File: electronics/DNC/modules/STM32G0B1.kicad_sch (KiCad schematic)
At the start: 1 part, among them U4 STM32G0B1RETx

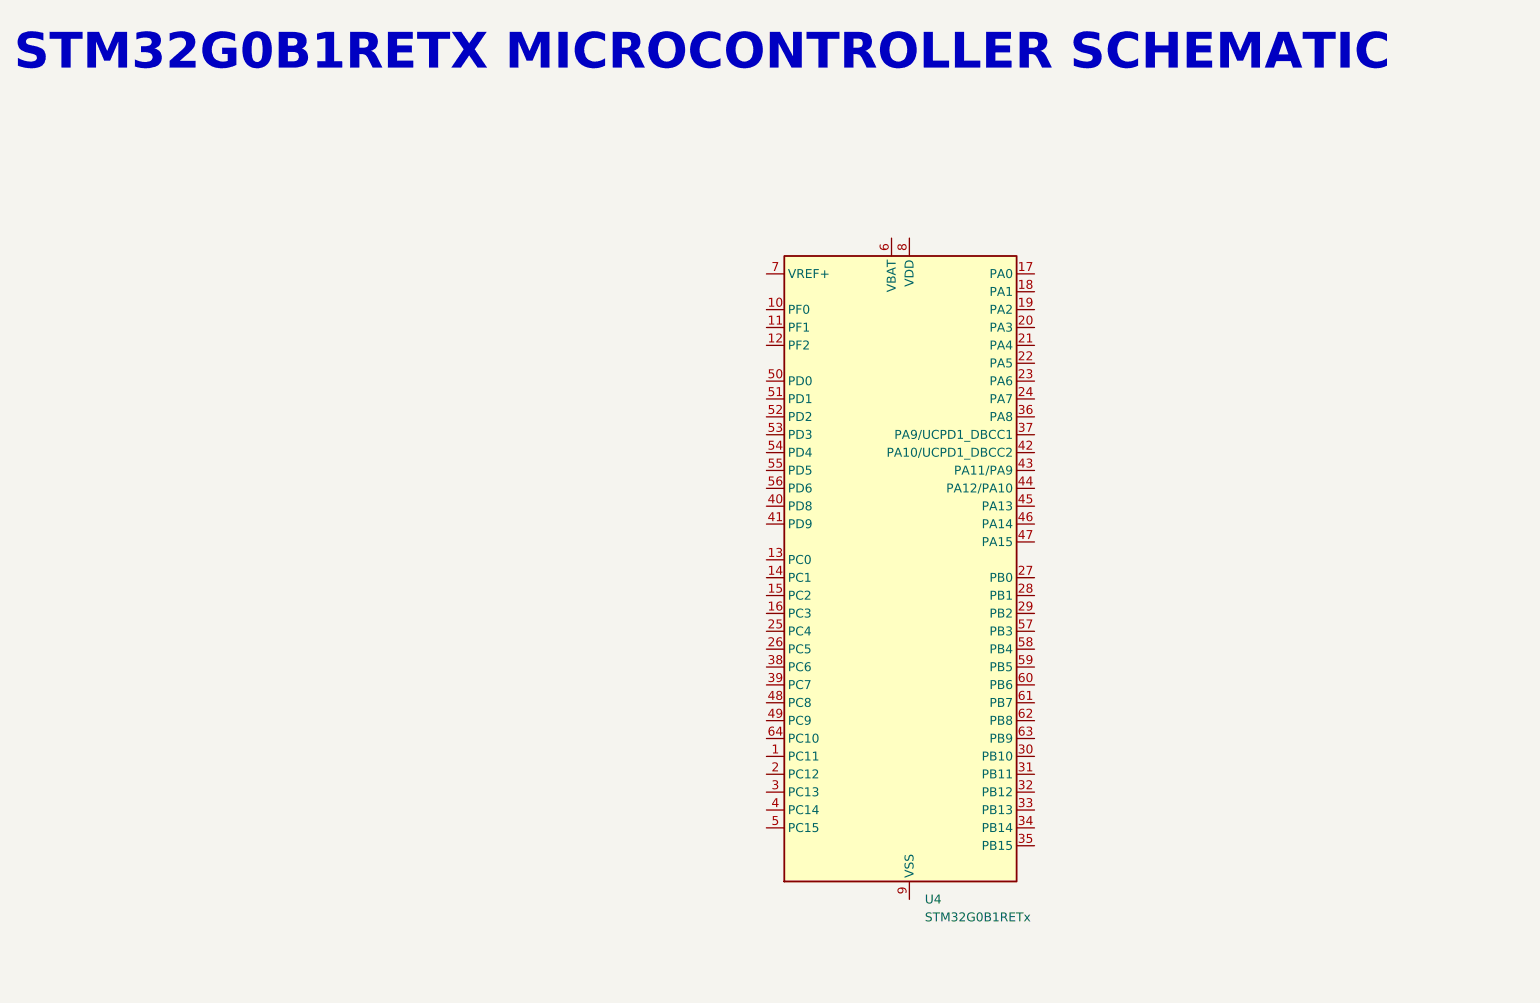
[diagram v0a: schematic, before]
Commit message: Se empezó de nuevo el diseño del DNC con una nueva arquitectura
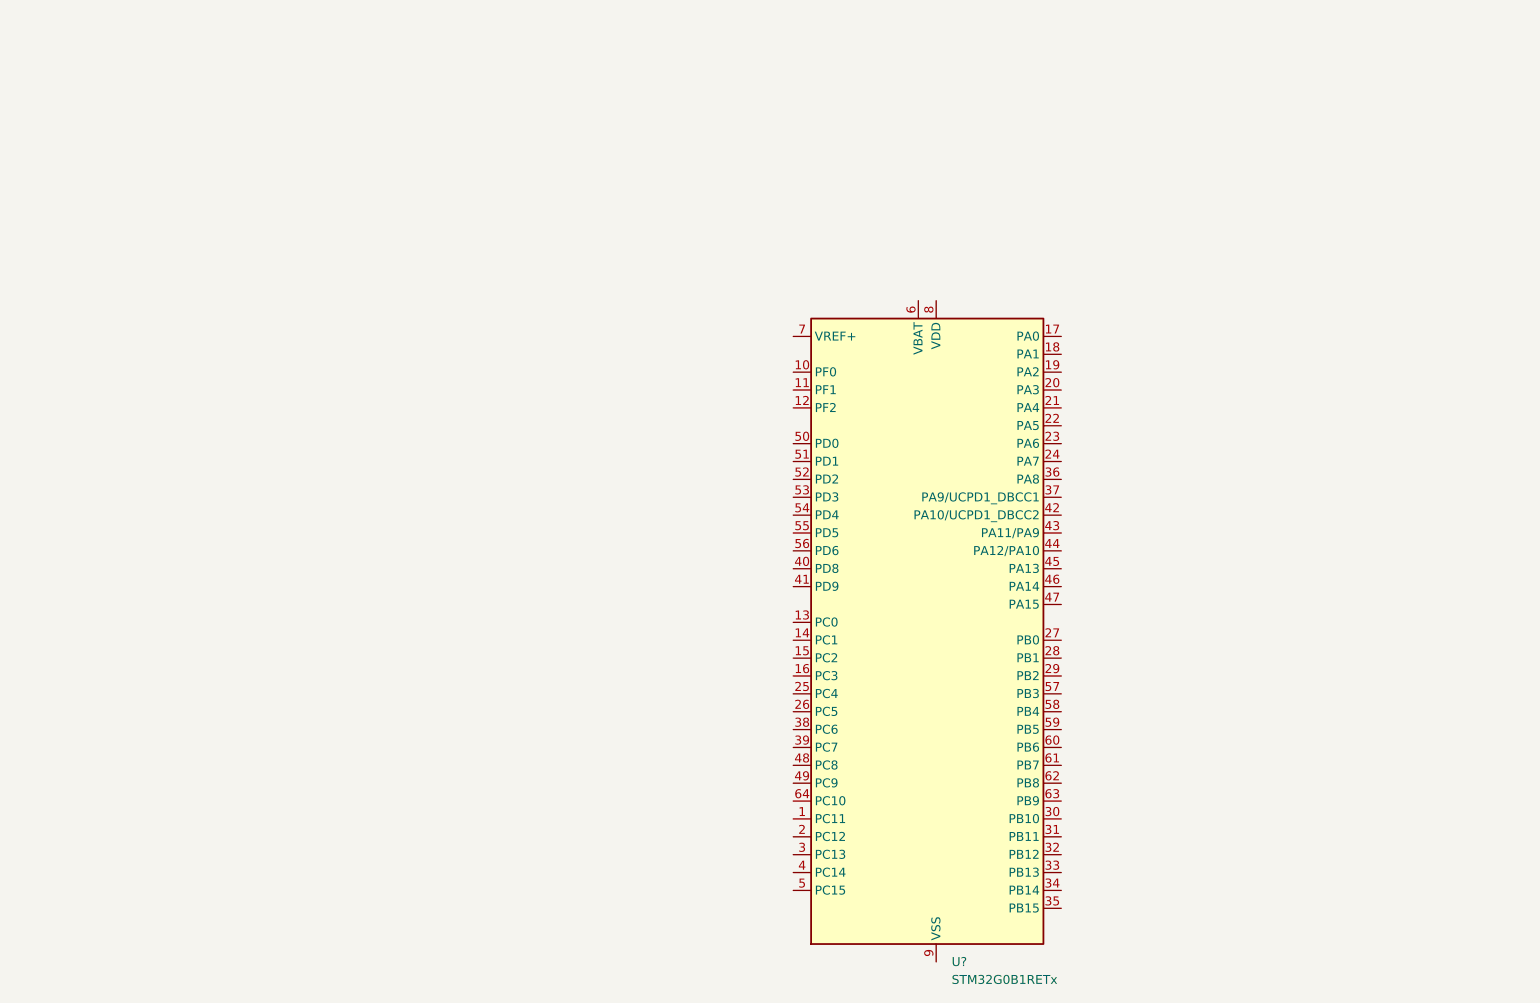
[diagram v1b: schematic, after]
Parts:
- removed U4: STM32G0B1RETx, Package_QFP:LQFP-64_10x10mm_P0.5mm, symbol MCU_ST_STM32G0:STM32G0B1RETx
- added U?: STM32G0B1RETx, Package_QFP:LQFP-64_10x10mm_P0.5mm, symbol MCU_ST_STM32G0:STM32G0B1RETx
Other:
- note removed: "STM32G0B1RETX MICROCONTROLLER SCHEMATIC"
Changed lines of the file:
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@@
 	(generator_version "8.0")
 	(paper "A4")
-	(text "STM32G0B1RETX MICROCONTROLLER SCHEMATIC"
-		(exclude_from_sim no)
-		(at 18.796 23.622 0)
-		(effects
-			(font
-				(size 5.08 5.08)
-				(thickness 1.016)
-				(bold yes)
-			)
-			(justify left bottom)
-		)
-	)
 	(symbol
 		(lib_id "MCU_ST_STM32G0:STM32G0B1RETx")
-		(at 143.51 95.25 0)
+		(at 147.32 104.14 0)
 		(unit 1)
 		(exclude_from_sim no)
@@
 		(dnp no)
 		(fields_autoplaced yes)
-		(property "Reference" "U4"
-			(at 148.2441 140.97 0)
+		(property "Reference" "U?"
+			(at 152.0541 149.86 0)
 			(effects
 				(font
@@
 		)
 		(property "Value" "STM32G0B1RETx"
-			(at 148.2441 143.51 0)
+			(at 152.0541 152.4 0)
 			(effects
 				(font
@@
 		)
 		(property "Footprint" "Package_QFP:LQFP-64_10x10mm_P0.5mm"
-			(at 128.27 138.43 0)
+			(at 132.08 147.32 0)
 			(effects
 				(font
@@
 		)
 		(property "Datasheet" "https://www.st.com/resource/en/datasheet/stm32g0b1re.pdf"
-			(at 143.51 95.25 0)
+			(at 147.32 104.14 0)
 			(effects
 				(font
@@
 		)
 		(property "Description" "STMicroelectronics Arm Cortex-M0+ MCU, 512KB flash, 144KB RAM, 64 MHz, 1.7-3.6V, 60 GPIO, LQFP64"
-			(at 143.51 95.25 0)
-			(effects
-				(font
-					(size 1.27 1.27)
-				)
-				(hide yes)
-			)
+			(at 147.32 104.14 0)
+			(effects
+				(font
+					(size 1.27 1.27)
+				)
+				(hide yes)
+			)
+		)
+		(property "Manufacturer" "STMicroelectronics"
+			(at 147.32 104.14 0)
+			(effects
+				(font
+					(size 1.27 1.27)
+				)
+				(hide yes)
+			)
+		)
+		(property "Mfg Part #" "STM32G0B1RET6"
+			(at 147.32 104.14 0)
+			(effects
+				(font
+					(size 1.27 1.27)
+				)
+				(hide yes)
+			)
+		)
+		(property "LCSC Part #" "C2829307"
+			(at 147.32 104.14 0)
+			(effects
+				(font
+					(size 1.27 1.27)
+				)
+				(hide yes)
+			)
+		)
+		(property "PROVIDER" "Digikey"
+			(at 147.32 104.14 0)
+			(effects
+				(font
+					(size 1.27 1.27)
+				)
+				(hide yes)
+			)
+		)
+		(property "Price" "5.31"
+			(at 147.32 104.14 0)
+			(effects
+				(font
+					(size 1.27 1.27)
+				)
+				(hide yes)
+			)
+		)
+		(property "Descrip" "IC MCU 32BIT 512KB FLASH 64LQFP"
+			(at 147.32 104.14 0)
+			(effects
+				(font
+					(size 1.27 1.27)
+				)
+				(hide yes)
+			)
+		)
+		(property "PLACE" ""
+			(at 147.32 104.14 0)
+			(effects
+				(font
+					(size 1.27 1.27)
+				)
+			)
+		)
+		(property "CURRENT" ""
+			(at 147.32 104.14 0)
+			(effects
+				(font
+					(size 1.27 1.27)
+				)
+			)
+		)
+		(property "TC" ""
+			(at 147.32 104.14 0)
+			(effects
+				(font
+					(size 1.27 1.27)
+				)
+			)
+		)
+		(property "Power" ""
+			(at 147.32 104.14 0)
+			(effects
+				(font
+					(size 1.27 1.27)
+				)
+			)
+		)
+		(property "Tol" ""
+			(at 147.32 104.14 0)
+			(effects
+				(font
+					(size 1.27 1.27)
+				)
+			)
+		)
+		(property "Sim.Device" ""
+			(at 147.32 104.14 0)
+			(effects
+				(font
+					(size 1.27 1.27)
+				)
+				(hide yes)
+			)
+		)
+		(property "Sim.Pins" ""
+			(at 147.32 104.14 0)
+			(effects
+				(font
+					(size 1.27 1.27)
+				)
+				(hide yes)
+			)
+		)
+		(pin "26"
+		)
+		(pin "36"
+		)
+		(pin "20"
+		)
+		(pin "12"
 		)
 		(pin "33"
 		)
+		(pin "44"
+		)
+		(pin "53"
+		)
+		(pin "59"
+		)
+		(pin "42"
+		)
+		(pin "47"
+		)
+		(pin "49"
+		)
+		(pin "25"
+		)
+		(pin "16"
+		)
+		(pin "3"
+		)
+		(pin "18"
+		)
+		(pin "29"
+		)
+		(pin "28"
+		)
+		(pin "5"
+		)
+		(pin "35"
+		)
+		(pin "40"
+		)
+		(pin "19"
+		)
+		(pin "41"
+		)
+		(pin "30"
+		)
+		(pin "15"
+		)
+		(pin "1"
+		)
+		(pin "14"
+		)
+		(pin "22"
+		)
+		(pin "46"
+		)
+		(pin "48"
+		)
 		(pin "51"
 		)
+		(pin "31"
+		)
+		(pin "32"
+		)
+		(pin "11"
+		)
+		(pin "21"
+		)
+		(pin "2"
+		)
 		(pin "17"
 		)
+		(pin "24"
+		)
+		(pin "27"
+		)
+		(pin "34"
+		)
+		(pin "37"
+		)
+		(pin "38"
+		)
+		(pin "23"
+		)
+		(pin "50"
+		)
+		(pin "43"
+		)
+		(pin "10"
+		)
 		(pin "54"
 		)
-		(pin "25"
-		)
-		(pin "29"
+		(pin "55"
+		)
+		(pin "13"
+		)
+		(pin "45"
+		)
+		(pin "39"
 		)
 		(pin "4"
 		)
-		(pin "18"
-		)
-		(pin "22"
-		)
-		(pin "27"
-		)
-		(pin "1"
-		)
-		(pin "10"
-		)
-		(pin "16"
-		)
-		(pin "3"
-		)
-		(pin "30"
-		)
-		(pin "36"
-		)
-		(pin "15"
-		)
-		(pin "19"
-		)
-		(pin "24"
-		)
-		(pin "14"
-		)
-		(pin "32"
-		)
-		(pin "2"
-		)
-		(pin "20"
-		)
-		(pin "26"
-		)
-		(pin "37"
-		)
-		(pin "38"
-		)
-		(pin "28"
-		)
-		(pin "41"
-		)
-		(pin "44"
-		)
-		(pin "45"
-		)
-		(pin "23"
-		)
-		(pin "13"
-		)
-		(pin "5"
-		)
-		(pin "40"
-		)
-		(pin "11"
-		)
-		(pin "21"
-		)
-		(pin "31"
-		)
-		(pin "42"
-		)
-		(pin "47"
-		)
-		(pin "34"
-		)
-		(pin "48"
-		)
-		(pin "50"
-		)
-		(pin "35"
-		)
-		(pin "39"
-		)
-		(pin "43"
-		)
-		(pin "46"
-		)
-		(pin "12"
-		)
-		(pin "49"
+		(pin "56"
+		)
+		(pin "57"
 		)
 		(pin "52"
 		)
-		(pin "53"
-		)
-		(pin "55"
-		)
 		(pin "58"
 		)
-		(pin "59"
-		)
 		(pin "6"
 		)
@@
 		(pin "61"
 		)
-		(pin "56"
-		)
 		(pin "62"
 		)
-		(pin "57"
-		)
 		(pin "63"
 		)
+		(pin "7"
+		)
+		(pin "8"
+		)
+		(pin "9"
+		)
 		(pin "64"
-		)
-		(pin "7"
-		)
-		(pin "8"
-		)
-		(pin "9"
 		)
 		(instances
 			(project ""
-				(path "/abee636e-ad3a-4ba4-b95f-d0cf4a6d3d85/a3f2e46a-cb9e-45e4-8ad1-ca6576695bbf"
-					(reference "U4")
+				(path "/abee636e-ad3a-4ba4-b95f-d0cf4a6d3d85/6aca0810-46ed-4e55-b6f9-564a2498f8e7"
+					(reference "U?")
 					(unit 1)
 				)
